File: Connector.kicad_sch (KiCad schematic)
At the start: 1 part, among them SW2 SW_SPDT

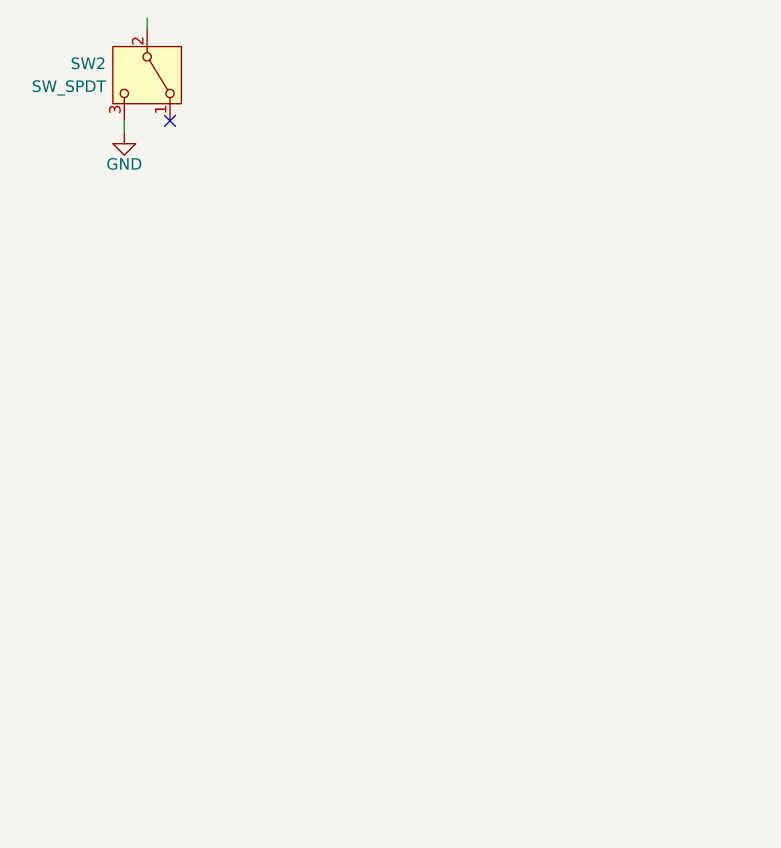
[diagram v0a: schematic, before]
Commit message: feat: add standardized functional notes across all schematic sheets
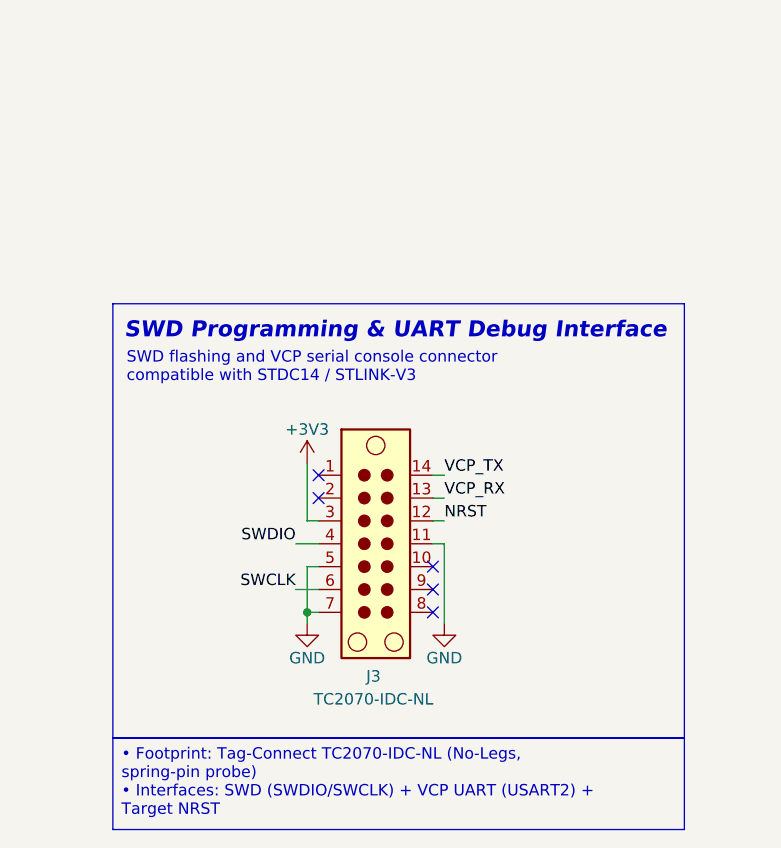
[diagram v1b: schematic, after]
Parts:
- removed SW2: SW_SPDT, Button_Switch_THT:SW_Slide_SPDT_Angled_CK_OS102011MA1Q, symbol Switch:SW_SPDT
- added J3: TC2070-IDC-NL, Library:Tag-Connect_TC2070-IDC-FP_2x07_P1.27mm_Vertical, symbol Connector:TC2070
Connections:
- net GND: now also J3.11, J3.5, J3.7
- new net +3V3: J3.3
- new net NRST: J3.12
- new net SWCLK: J3.6
- new net SWDIO: J3.4
- new net VCP_RX: J3.13
- new net VCP_TX: J3.14
- no-connect marks 1 -> 5
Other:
- note added: "SWD Programming & UART Debug Interface"
- note added: "SWD flashing and VCP serial console connector compatible with STDC14 / STLINK-V3"
- title: (none) -> KinetiCoreDC - Connector

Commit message: fix: fix some errors in shematic
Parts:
- added C27: 100nF, Capacitor_SMD:C_0603_1608Metric, symbol Device:C_Small
- added J2: Conn_01x04, Connector_Wire:SolderWire-1sqmm_1x04_P7.8mm_D1.4mm_OD3.9mm_Relief, symbol Connector_Generic:Conn_01x04
- added J3: Conn_01x04, Connector_JST:JST_XH_S4B-XH-A-1_1x04_P2.50mm_Horizontal, symbol Connector_Generic:Conn_01x04
- added R52, R53: 100R, Resistor_SMD:R_0603_1608Metric, symbol Device:R_Small
- added SW2: OS102011MA1Q, Button_Switch_THT:SW_Slide_SPDT_Angled_CK_OS102011MA1Q, symbol Switch:SW_SPDT
- added U13: 74LVC2G126, Package_SO:VSSOP-8_2.3x2mm_P0.5mm, symbol 74xGxx:74LVC2G126
- J1: renamed from J3; footprint Library:Tag-Connect_TC2070-IDC-FP_2x07_P1.27mm_Vertical -> KineticCore:Tag-Connect_TC2070-IDC-FP_2x07_P1.27mm_Vertical
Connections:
- net +3V3: now also C27.1, U13.8 (VCC)
- net GND: now also C27.2, SW2.3 (C), U13.4 (GND)
- new net: R53.1, U13.2
- new net: R52.1, U13.3
- new net RX_EXT: U13.6
- new net RX_MCU: R52.2
- new net SHDN_EXT: SW2.2 (B)
- new net TX_EXT: U13.5
- new net TX_MCU: R53.2
- no-connect marks 5 -> 6
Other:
- note added: "Manual Power Enable"
- note added: "On-board SPDT slide switch for manual power shutdown and sleep mode (< 10 µA)."
- moved on the sheet: J1

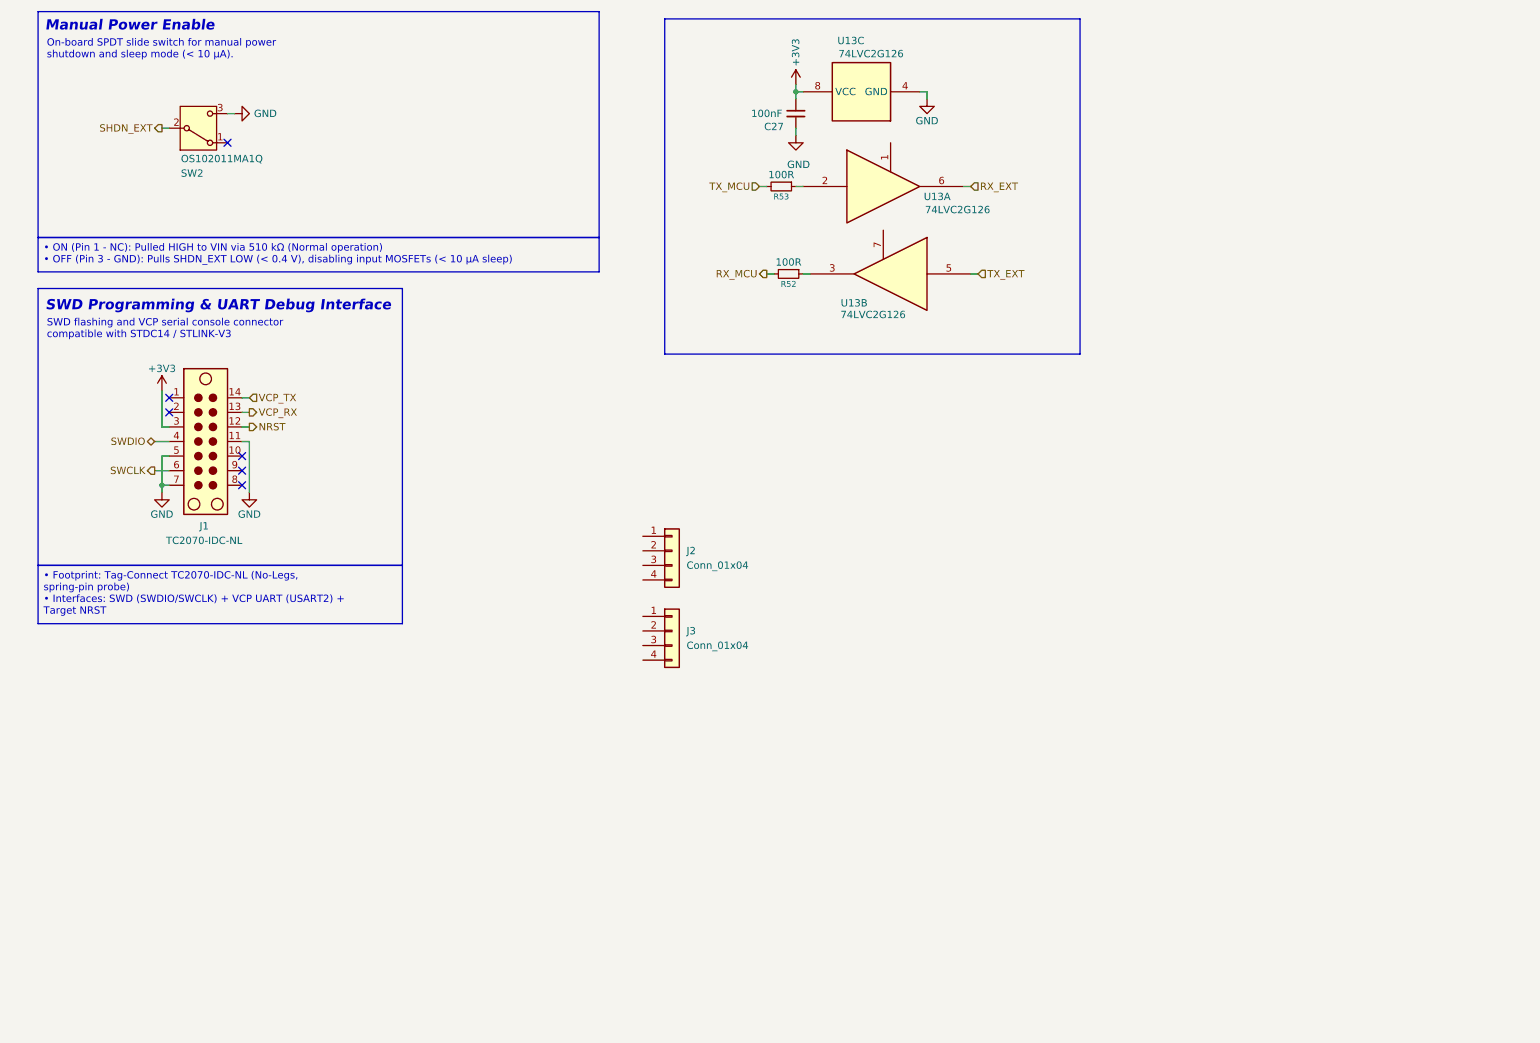
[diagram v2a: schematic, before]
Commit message: wip(sch): draft JST-XH and solder pad connector interfaces
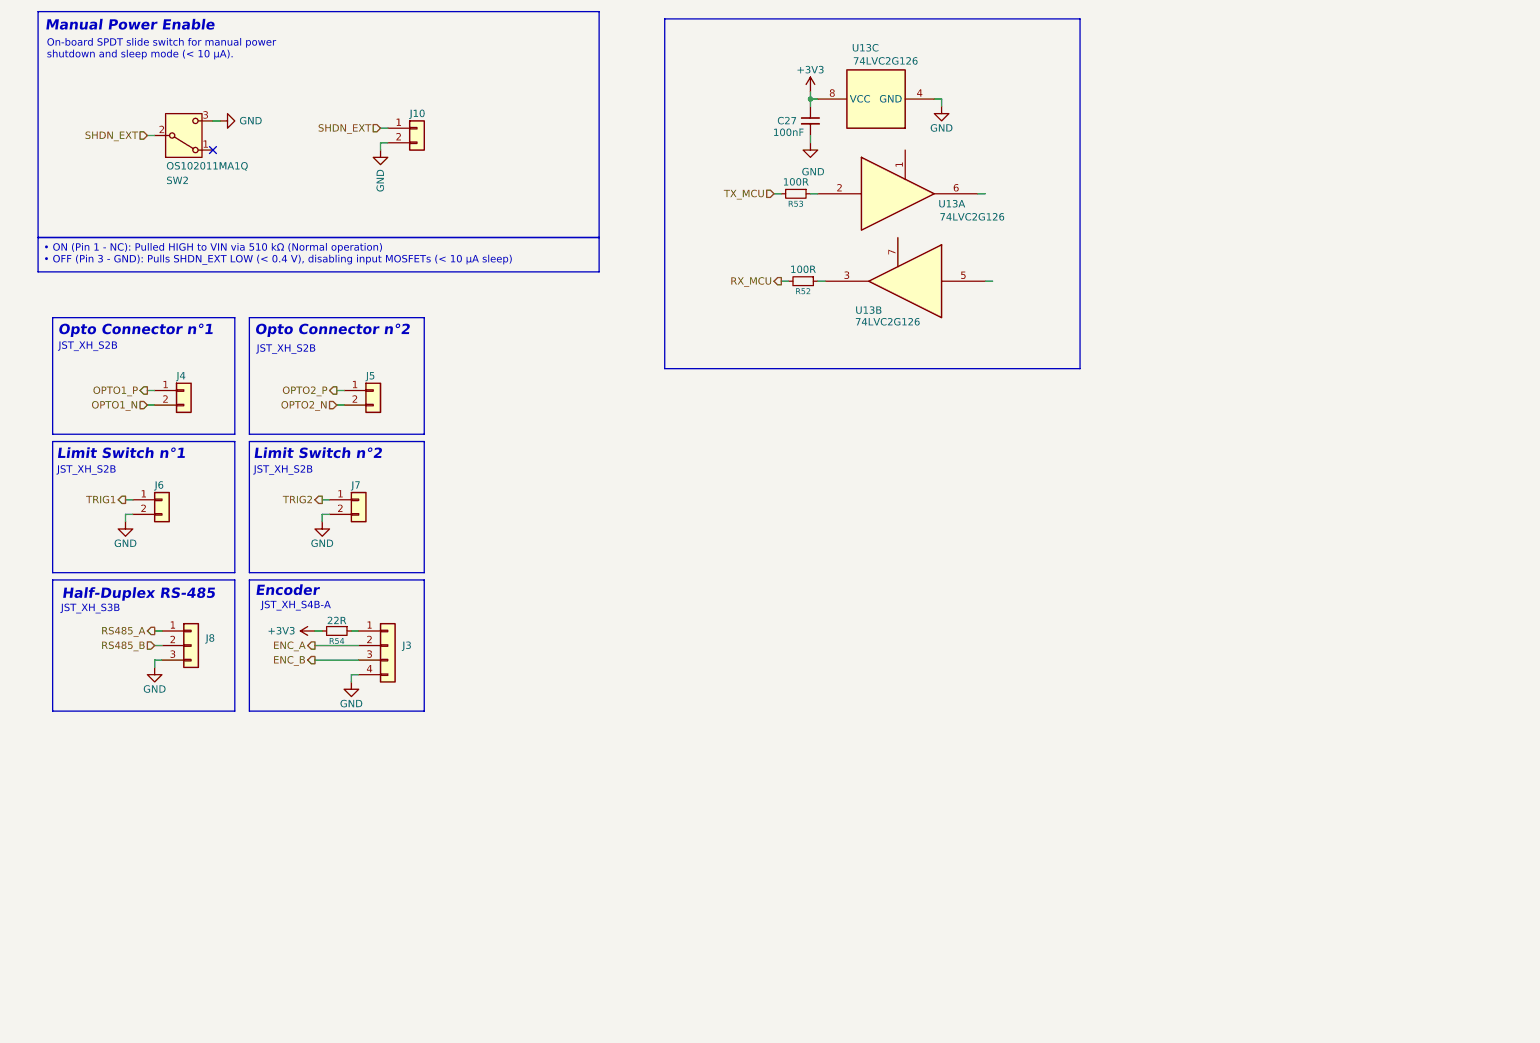
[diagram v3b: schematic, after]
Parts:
- removed J1: TC2070-IDC-NL, KineticCore:Tag-Connect_TC2070-IDC-FP_2x07_P1.27mm_Vertical, symbol Connector:TC2070
- removed J2: Conn_01x04, Connector_Wire:SolderWire-1sqmm_1x04_P7.8mm_D1.4mm_OD3.9mm_Relief, symbol Connector_Generic:Conn_01x04
- added J10, J4, J5, J6, J7: JST_XH_S2B-A, Connector_JST:JST_XH_S2B-XH-A_1x02_P2.50mm_Horizontal, symbol Connector_Generic:Conn_01x02
- added J8: JST_XH_S3B, Connector_JST:JST_XH_S3B-XH-A-1_1x03_P2.50mm_Horizontal, symbol Connector_Generic:Conn_01x03
- added R54: 22R, Resistor_SMD:R_0603_1608Metric, symbol Device:R_Small
- J3: value Conn_01x04 -> JST_XH_S4B-A
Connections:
- net +3V3: now also R54.2
- net GND: now also J3.4 (Pin_4), J10.2 (Pin_2), J6.2 (Pin_2), J7.2 (Pin_2), J8.3 (Pin_3)
- net SHDN_EXT: now also J10.1 (Pin_1)
- net at J3.1 (Pin_1): now also R54.1
- net ENC_A: now reaches J3.2 (Pin_2)
- net ENC_B: now reaches J3.3 (Pin_3)
- net RX_EXT: no longer names the net of U13.6
- net TX_EXT: no longer names the net of U13.5
- new net OPTO1_N: J4.2 (Pin_2)
- new net OPTO1_P: J4.1 (Pin_1)
- new net OPTO2_N: J5.2 (Pin_2)
- new net OPTO2_P: J5.1 (Pin_1)
- new net RS485_A: J8.1 (Pin_1)
- new net RS485_B: J8.2 (Pin_2)
- new net TRIG1: J6.1 (Pin_1)
- new net TRIG2: J7.1 (Pin_1)
- no-connect marks 6 -> 1
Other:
- note added: "Encoder"
- note added: "Half-Duplex RS-485"
- note added: "JST_XH_S2B"
- note added: "JST_XH_S3B"
- note added: "JST_XH_S4B-A"
- note added: "Limit Switch n°1"
- note added: "Limit Switch n°2"
- note added: "Opto Connector n°1"
- note added: "Opto Connector n°2"
- note removed: "SWD Programming & UART Debug Interface"
- note removed: "SWD flashing and VCP serial console connector compatible with STDC14 / STLINK-V3"
- moved on the sheet: C27, J3, R52, R53, SW2, U13A, U13B, U13C

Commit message: fix: FIx some modification
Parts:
- added J9: JST_XH_S4B-A, Connector_JST:JST_XH_S4B-XH-A-1_1x04_P2.50mm_Horizontal, symbol Connector_Generic:Conn_01x04
- added R55, R56: 10K, Resistor_SMD:R_0603_1608Metric, symbol Device:R_Small
- added R57, R58, R59: 22R, Resistor_SMD:R_0603_1608Metric, symbol Device:R_Small
- added U14: WE-TVS-82400102, Package_TO_SOT_SMD:SOT-23-6, symbol Power_Protection:WE-TVS-82400102
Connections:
- net +3V3: now also R55.2, R56.2, R57.2
- net GND: now also J9.4 (Pin_4), U14.2
- net at R53.1, U13.2: now also R55.1
- net at U13.1: now also R59.1
- net at U13.6: now also U14.6
- net at R52.1, U13.3: now also R56.1
- net at U13.5: now also U14.4
- net at U13.7: now also R58.2
- new net: J9.1 (Pin_1), R57.1
- new net OE_MCU: R58.1, R59.2
- new net RX_EXT: J9.2 (Pin_2), U14.1
- new net TX_EXT: J9.3 (Pin_3), U14.3
- no-connect marks 1 -> 2
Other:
- note added: "UART"
- moved on the sheet: J10, J4, J5, J6, J7, J8, R52, R53, SW2, U13A, U13B, U13C

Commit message: refactor(schematic): migrate MCU to LQFP48 and finalize pinout mapping
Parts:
- removed C27: 100nF, Capacitor_SMD:C_0603_1608Metric, symbol Device:C_Small
- removed R52, R53: 100R, Resistor_SMD:R_0603_1608Metric, symbol Device:R_Small
- removed R55, R56: 10K, Resistor_SMD:R_0603_1608Metric, symbol Device:R_Small
- removed R58, R59: 22R, Resistor_SMD:R_0603_1608Metric, symbol Device:R_Small
- removed U13: 74LVC2G126, Package_SO:VSSOP-8_2.3x2mm_P0.5mm, symbol 74xGxx:74LVC2G126
- removed U14: WE-TVS-82400102, Package_TO_SOT_SMD:SOT-23-6, symbol Power_Protection:WE-TVS-82400102
- added J1: TC2070-IDC-NL, KineticCore:Tag-Connect_TC2070-IDC-FP_2x07_P1.27mm_Vertical, symbol Connector:TC2070
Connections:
- net +3V3: now also J1.3
- net GND: now also J1.11, J1.5, J1.7
- net RX_EXT renamed VPC_RX_EXT
- net TX_EXT renamed VPC_TX_EXT
- new net NRST_MCU: J1.12
- new net SWCLK_MCU: J1.6
- new net SWDIO_MCU: J1.4
- new net VPC_RX_MCU: J1.13
- new net VPC_TX_MCU: J1.14
- no-connect marks 2 -> 6
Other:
- note added: "SWD Programming & UART Debug Interface"
- note added: "SWD flashing and VCP serial console connector compatible with STDC14 / STLINK-V3"
- moved on the sheet: J10

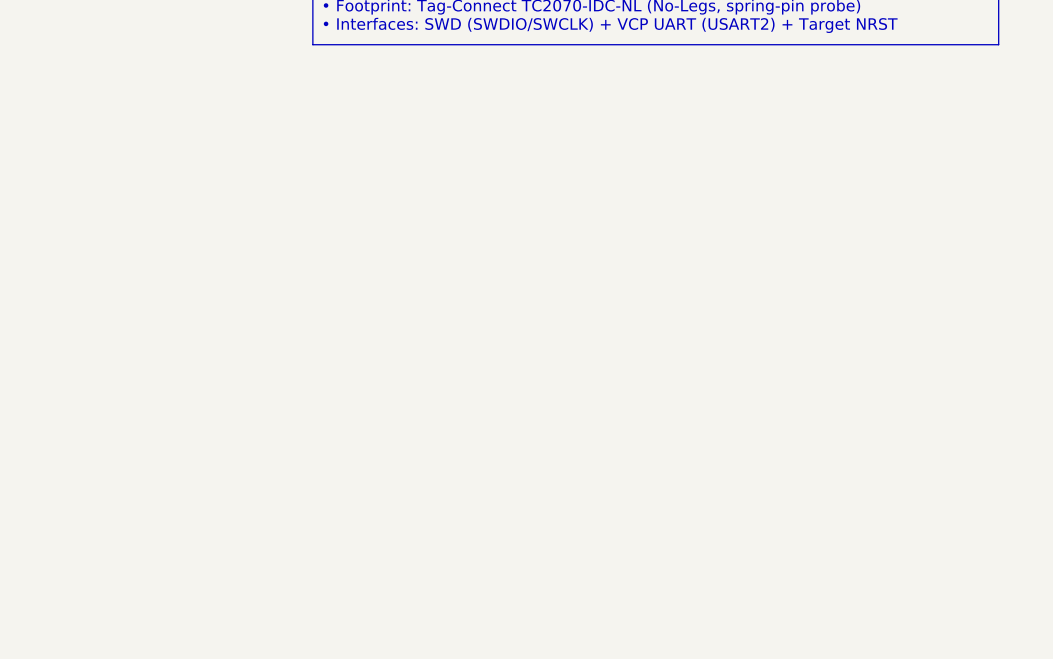
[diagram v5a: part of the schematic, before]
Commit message: feat: add XT30PW-M DC input connector with functional notes
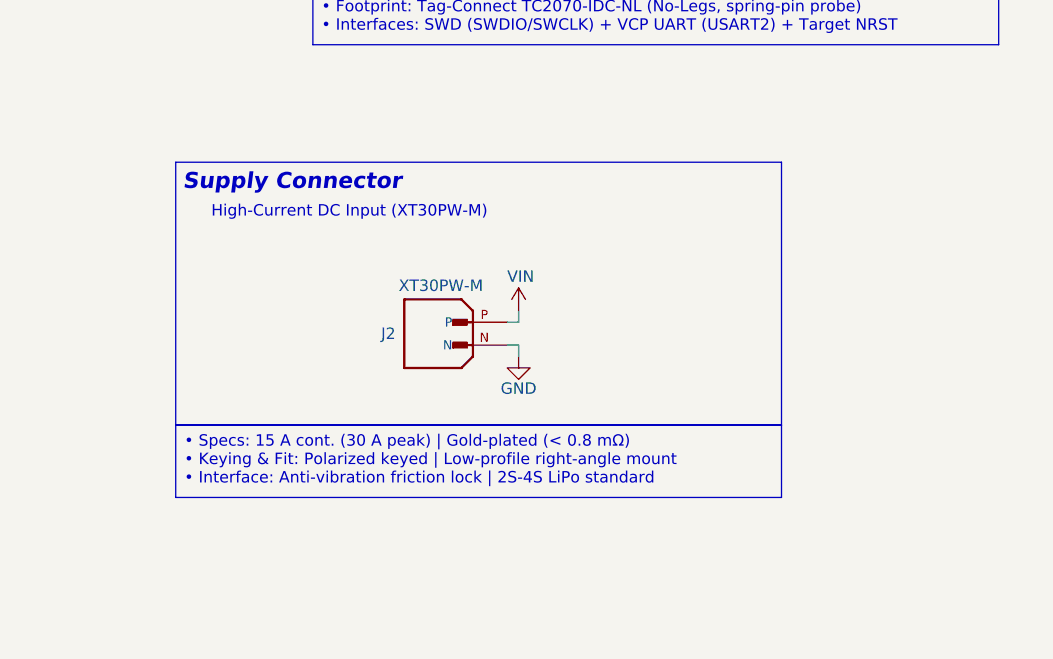
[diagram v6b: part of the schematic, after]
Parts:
- added J2: XT30PW-M, KineticCore:AMASS_XT30PW-M, symbol KineticCore:XT30PW-M
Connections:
- net GND: now also J2.N
- new net VIN: J2.P
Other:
- note added: "High-Current DC Input (XT30PW-M)"
- note added: "Supply Connector"
